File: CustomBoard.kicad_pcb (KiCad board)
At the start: 2 copper layers, 40.9 x 34.1 mm, 24 parts, among them J1 RIGHT, J10 Sensor08, J11 Sensor09, J12 Sensor10, J13 Sensor11, J14 Sensor12, J2 LEFT, J3 Sensor01, J4 Sensor02, J5 Sensor03, J6 Sensor04, J7 Sensor05, J8 Sensor06, J9 Sensor07, U1 DS28E05, U2 PCA9555, U3 VL53L1X

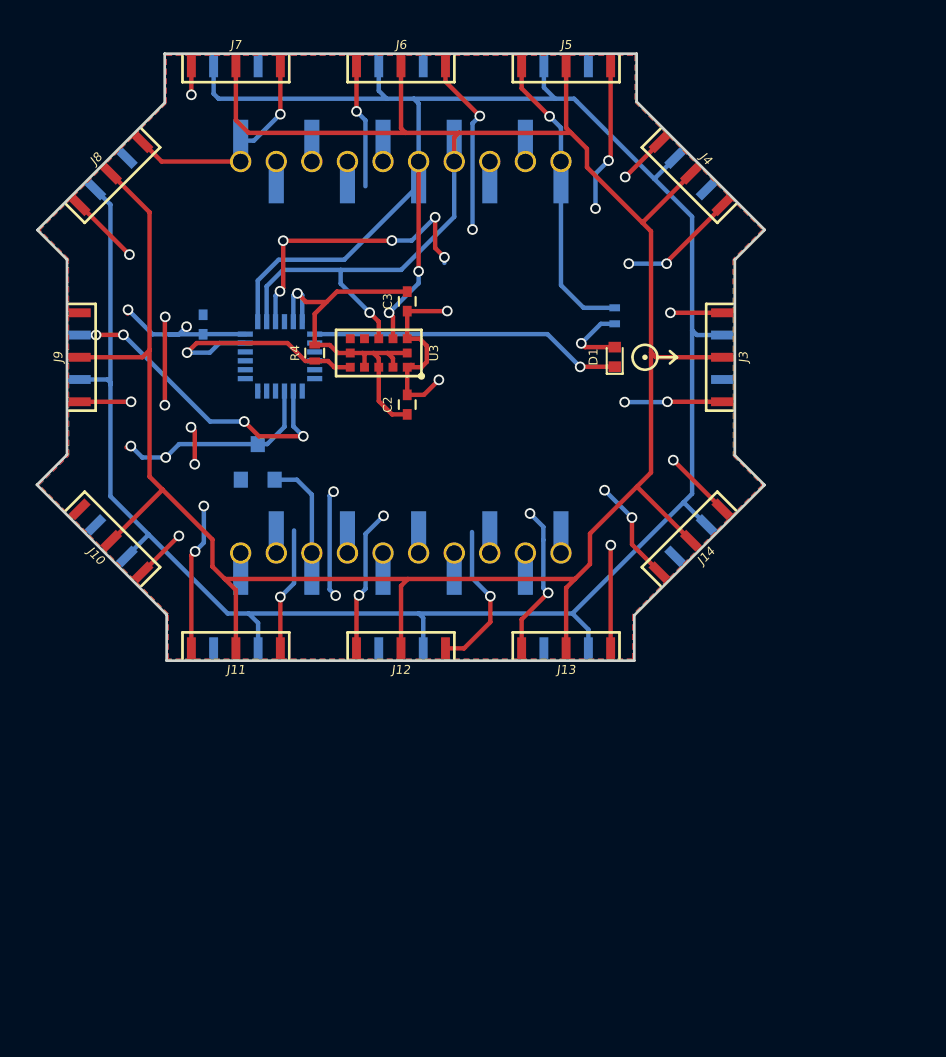
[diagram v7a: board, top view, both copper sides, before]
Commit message: adding 4 layers
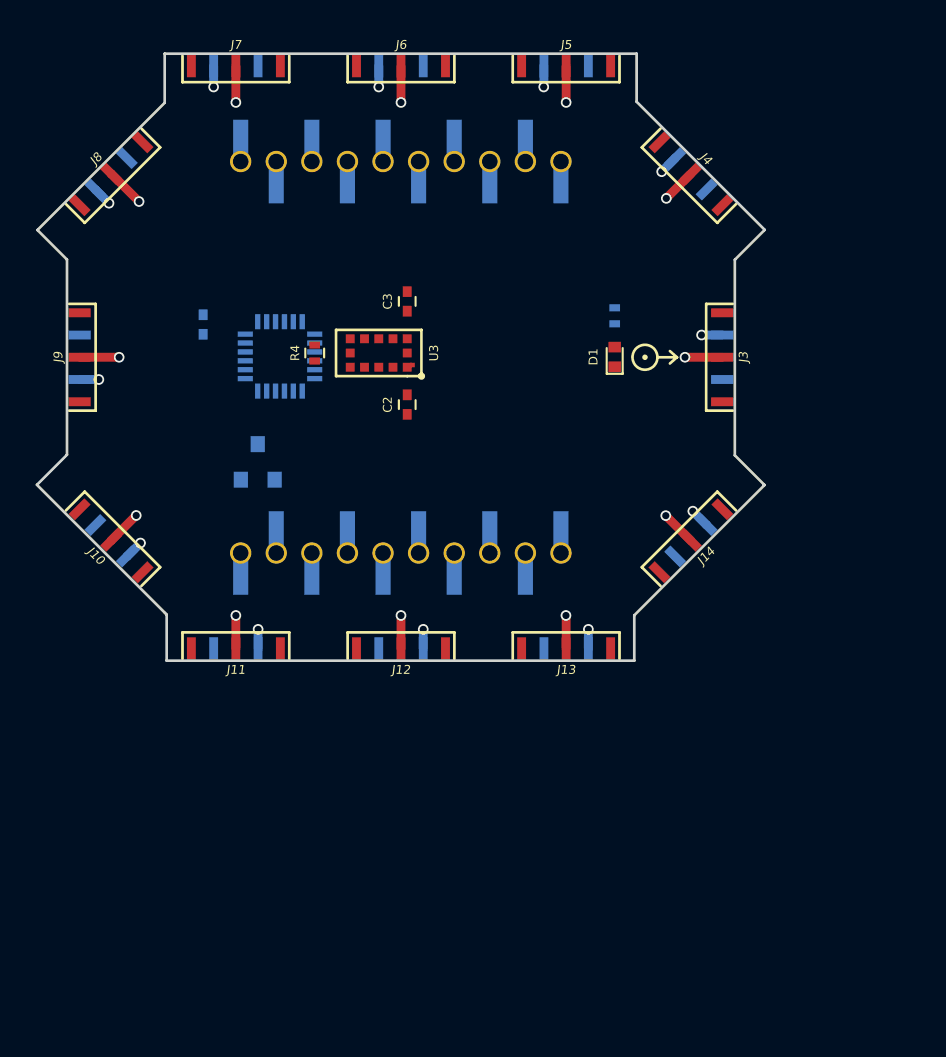
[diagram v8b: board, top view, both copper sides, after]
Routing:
- net GND: track 118.5 -> 0.00 mm, vias 22 -> 0
- net VCC: track 94.6 -> 0.00 mm, vias 19 -> 0
- net SDA: track 160.3 -> 122.2 mm, vias 1 -> 12
- net SCL: track 152.9 -> 132.8 mm, vias 2 -> 12
- net S07: track 17.7 -> 0.00 mm, vias 4 -> 0
- net Net-(D1-Pad1): track 17.6 -> 0.00 mm, vias 1 -> 0
- net (no net): track 13.5 -> 0.00 mm, vias 6 -> 0
- net S15: track 13.5 -> 0.00 mm, vias 1 -> 0
- net OW: track 5.72 -> 0.00 mm
- net Net-(D1-Pad2): track 4.30 -> 0.00 mm, vias 1 -> 0
- removed copper zone on F.Cu, net GND
- removed copper zone on B.Cu, net VCC
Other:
- copper layers 2 -> 4
